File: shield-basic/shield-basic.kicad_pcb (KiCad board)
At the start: 2 copper layers, 53 x 59 mm, 58 parts, among them CON1 SD_Card, IC1 DRV8833, P1 CONN_01X04, P2 CONN_01X04, P3 CONN_01X04, P4 CONN_01X04, P5 CONN_01X04, P6 CONN_01X02, P7 CONN_01X02, P8 CONN_01X06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

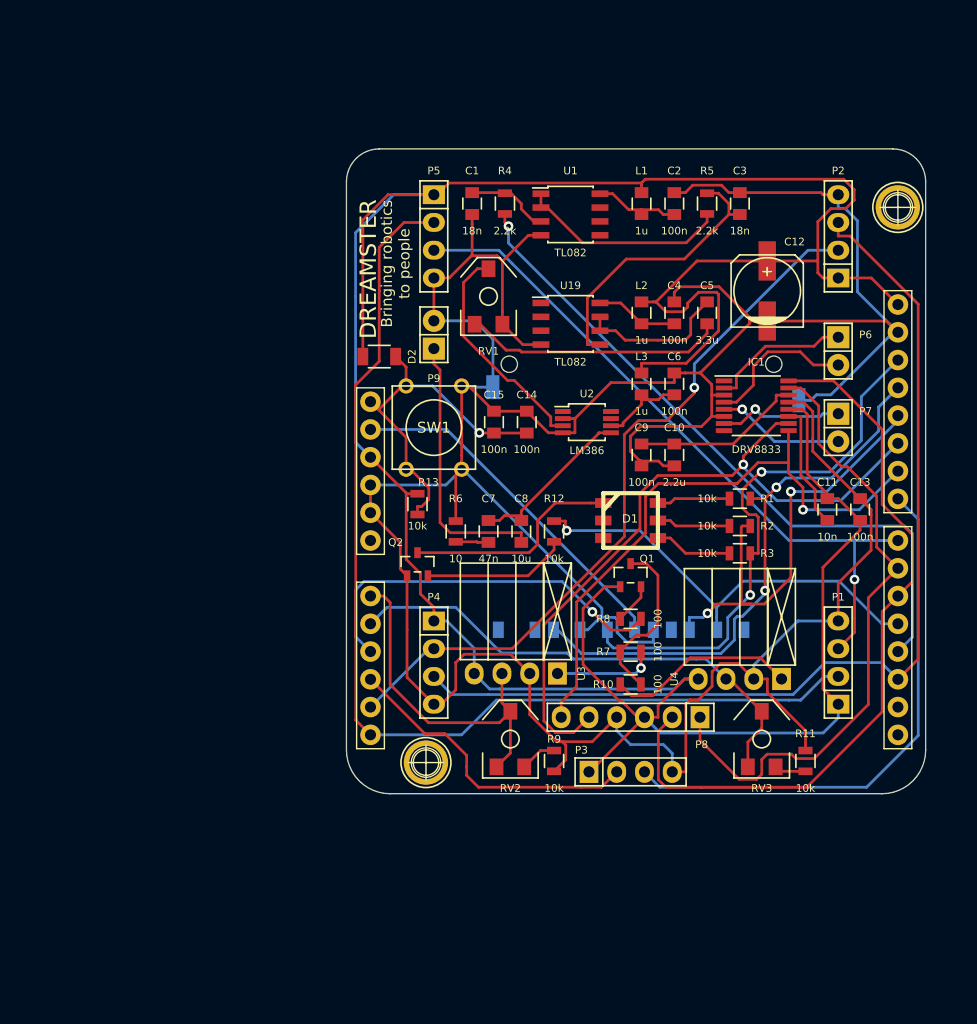
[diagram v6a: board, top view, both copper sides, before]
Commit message: The board is routed again, to fix some problems.
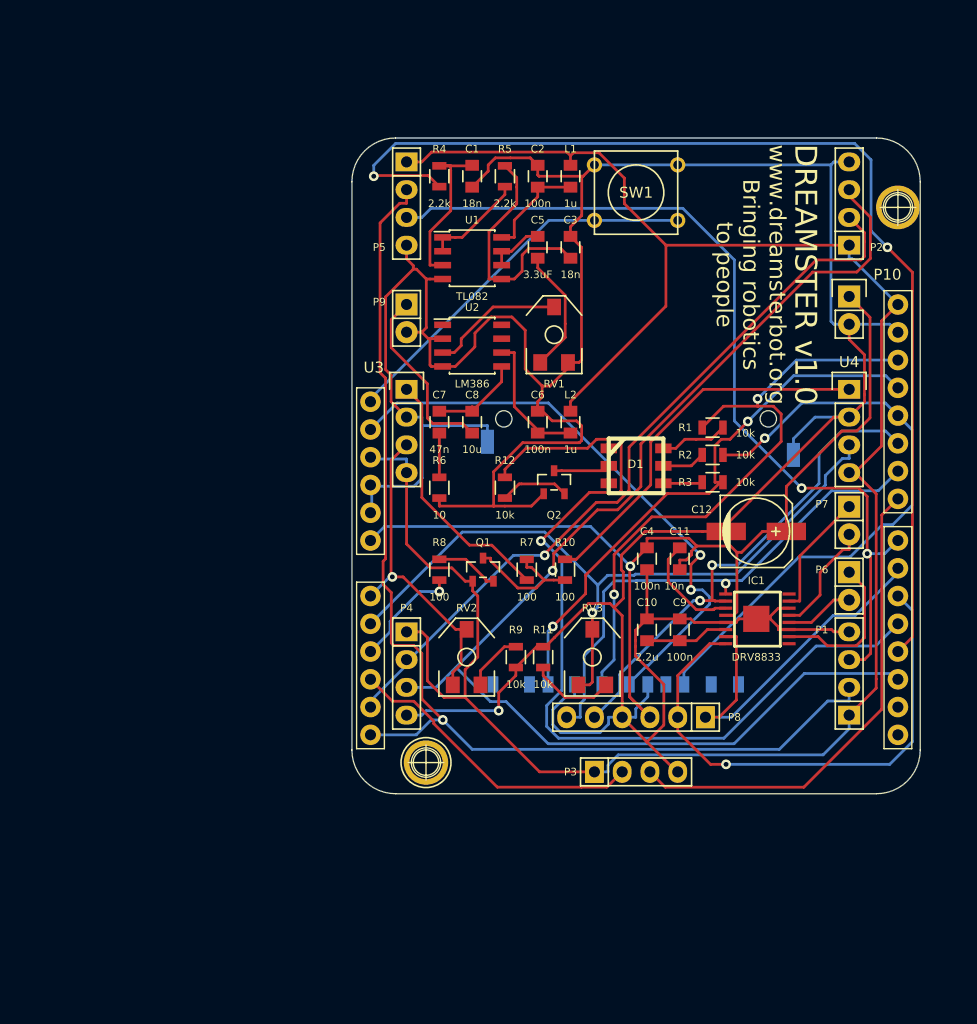
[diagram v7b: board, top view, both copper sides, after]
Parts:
- removed the 1pin at (197.9, 48.4)
- removed the 1pin at (154.8, 99.2)
- removed C13, C14, C15: 100n, Capacitors_SMD:C_0805
- removed D2: CD1206-S01575, Capacitors_SMD:C_1206
- removed L3: 1u, Capacitors_SMD:C_0805
- removed R13: 10k, Resistors_SMD:R_0805
- removed U19: TL082, Housings_SOIC:SOIC-8_3.9x4.9mm_Pitch1.27mm
- added 1pin: VAL**, Connect:1pin, F.Cu at (198.0, 48.4)
- added 1pin: VAL**, Connect:1pin, F.Cu at (154.8, 99.2)
- added P10: CONN_01X02, Socket_Strips:Socket_Strip_Straight_1x02, F.Cu at (193.5, 56.5)
- C5: value 3.3u -> 3.3uF
- IC1: footprint Housings_SSOP:TSSOP-16_4.4x5mm_Pitch0.65mm -> Dreamster:drv8833
- Q1: value PNP -> BC857
- Q2: value NPN -> BC847
- U2: footprint Housings_SSOP:MSOP-8_3x3mm_Pitch0.65mm -> Housings_SOIC:SOIC-8_3.9x4.9mm_Pitch1.27mm
- U3, U4: footprint Socket_Strips:Socket_Strip_Angled_1x04 -> Socket_Strips:Socket_Strip_Straight_1x04
- moved SW1 28.4 mm to (174.0, 47.0), turned to 180 degrees
- moved U4 28.3 mm to (193.5, 65.0), turned to 270 degrees
- moved U3 27.9 mm to (153.0, 65.0), turned to 270 degrees
- moved R11 25.8 mm to (165.5, 89.5)
- moved C4 22.6 mm to (175.0, 80.5), turned to 270 degrees
- moved C12 22.0 mm to (185.0, 78.0), turned to 0 degrees
- moved P6 21.5 mm to (193.5, 83.0)
- moved IC1 19.5 mm to (185.0, 86.0), turned to 90 degrees
- moved R5 18.7 mm to (162.0, 45.5)
- moved R8 18.1 mm to (156.0, 81.5), turned to 270 degrees
- moved RV3 17.2 mm to (170.0, 89.5)
- moved C5 16.6 mm to (165.0, 52.0)
- moved C9 16.4 mm to (178.0, 87.0), turned to 90 degrees
- moved C10 16.2 mm to (175.0, 87.0), turned to 90 degrees
- moved C3 16.0 mm to (168.0, 52.0)
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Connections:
- C11 pad 1: +5VD -> +BATT
- C12 pad 1: +5VD -> +BATT
- C4 pad 1: Net-(C4-Pad1) -> +BATT
- CON1 pad 1: /LED_enable -> (no net)
- IC1 pad 12: +5VD -> +BATT
- L2 pad 2: Net-(C4-Pad1) -> Net-(C6-Pad1)
- P8 pad 3: +5VD -> +BATT
- R1 pad 1: /RED -> /BLUE
- R3 pad 1: /BLUE -> /RED
- U1 pad 5: (no net) -> Net-(C3-Pad1)
- U1 pad 6: (no net) -> Net-(C5-Pad1)
- U1 pad 7: (no net) -> Net-(C5-Pad1)
- U5 pad VIN: (no net) -> +BATT
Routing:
- net +BATT: track 0.00 -> 96.3 mm, vias 0 -> 1
- net +5VD: track 277.6 -> 195.9 mm
- net /LED_enable: track 39.8 -> 81.7 mm
- net /sound/In: track 62.1 -> 101.5 mm, vias 1 -> 2
- net /irsensor/~EMITTER: track 34.9 -> 10.2 mm
- net /hbridge/RMI2: track 58.1 -> 33.8 mm
- net /ECHO_B: track 91.2 -> 115.2 mm, vias 0 -> 1
- net +3V3: track 32.4 -> 53.6 mm, vias 0 -> 2
- net /irsensor/RSENS: track 46.5 -> 66.3 mm, vias 0 -> 1
- net /hbridge/LMI2: track 64.1 -> 44.8 mm, vias 1 -> 2
- net /hbridge/RMI1: track 68.4 -> 49.3 mm, vias 0 -> 1
- net /ECHO_C: track 64.0 -> 82.1 mm, vias 1 -> 2
- net Net-(R10-Pad2): track 17.4 -> 34.7 mm
- net Net-(D1-Pad1): track 24.3 -> 8.20 mm
- net /GREEN: track 41.4 -> 55.6 mm, vias 2 -> 1
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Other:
- board size 53 x 59 mm -> 52 x 60 mm
- board text added: "DREAMSTER v1.0"
- board text added: "www.dreamsterbot.org Bringing robotics to people"
- board text removed: "Bringing robotics to people"
- board text removed: "DREAMSTER"

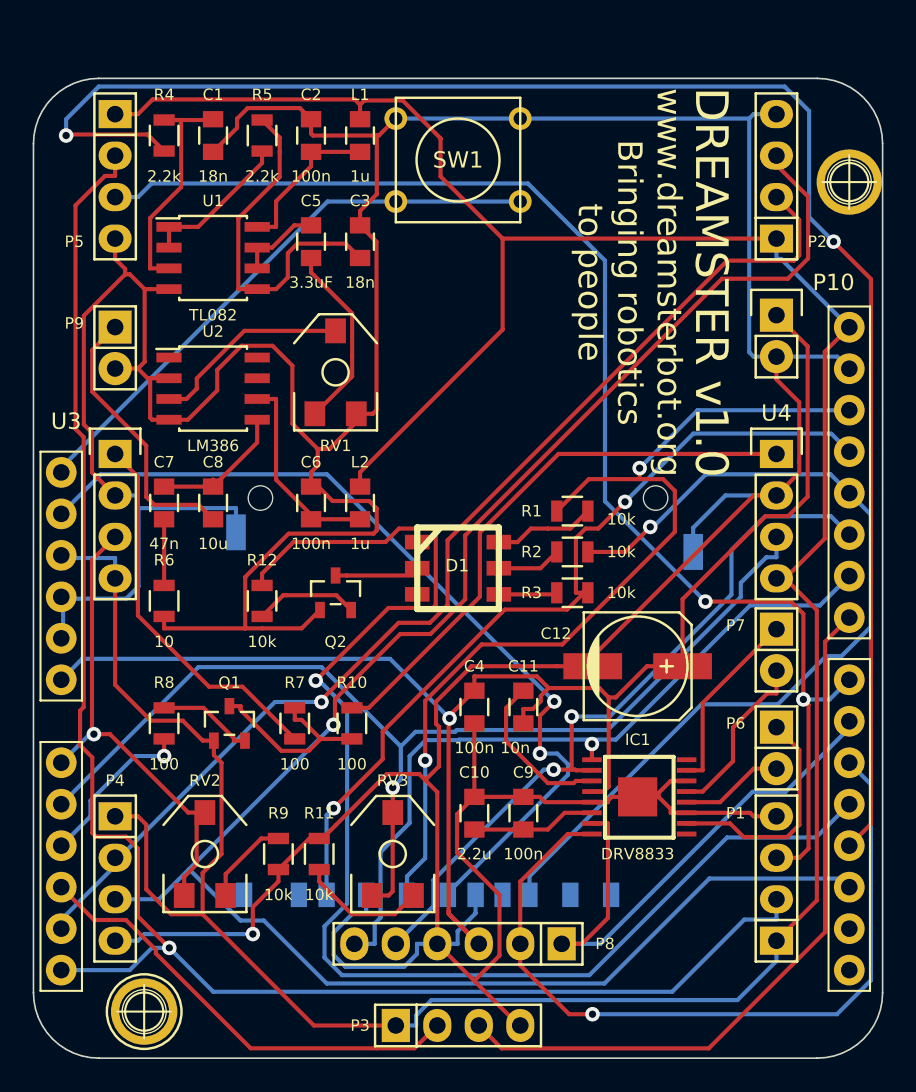
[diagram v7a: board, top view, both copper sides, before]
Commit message: Fix: #6 Add Gnd Plane. Fix: #9 Change IR footprint. Fix: #10 Move the trimmer, the orientation is ok.
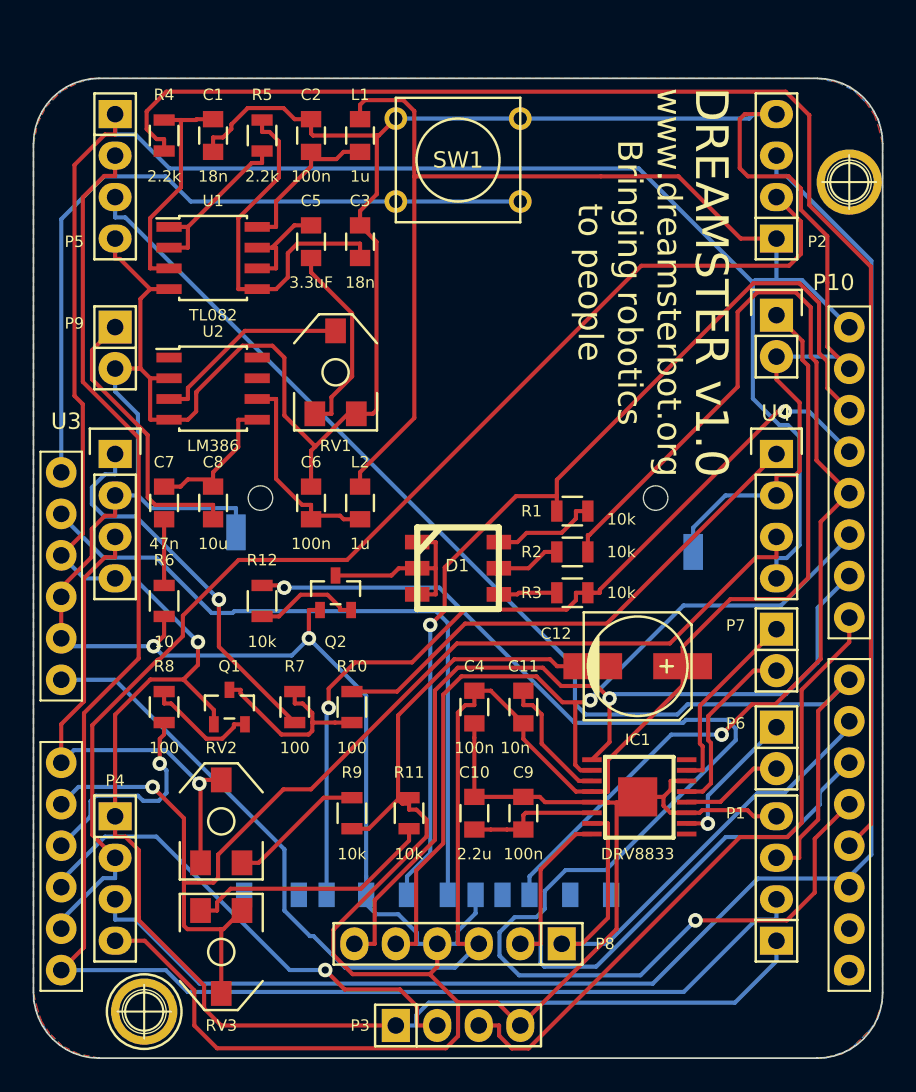
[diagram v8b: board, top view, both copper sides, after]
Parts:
- moved RV3 12.1 mm to (159.5, 95.5), turned to 180 degrees
- moved R11 6.04 mm to (171.0, 87.0)
- moved R9 5.15 mm to (167.5, 87.0)
- moved RV2 2.24 mm to (159.5, 87.5)
- moved Q1 1.00 mm to (160.0, 80.5)
- moved R10 1.00 mm to (167.5, 80.5)
- moved R7 1.00 mm to (164.0, 80.5)
- moved R8 1.00 mm to (156.0, 80.5)
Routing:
- net +5VD: track 195.9 -> 237.5 mm, vias 0 -> 1
- net /ECHO_B: track 115.2 -> 98.7 mm, vias 1 -> 0
- net /GREEN: track 55.6 -> 71.6 mm
- net /hbridge/RMI1: track 49.3 -> 36.9 mm, vias 1 -> 0
- net +3V3: track 53.6 -> 43.2 mm, vias 2 -> 0
- net /RESET: track 35.1 -> 45.3 mm
- net /sound/In: track 101.5 -> 91.7 mm, vias 2 -> 0
- net /hbridge/LMI1: track 46.3 -> 54.3 mm
- net /hbridge/LMI2: track 44.8 -> 52.6 mm, vias 2 -> 1
- net Net-(R11-Pad1): track 7.80 -> 15.6 mm
- net /ECHO_C: track 82.1 -> 74.6 mm, vias 2 -> 0
- net GND: track 332.7 -> 338.8 mm, vias 1 -> 2
- net /TRG_B: track 69.5 -> 75.0 mm, vias 1 -> 0
- net +BATT: track 96.3 -> 101.6 mm, vias 1 -> 0
- net /hbridge/RM+: track 14.1 -> 8.95 mm, vias 0 -> 1
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- added copper zone on B.Cu, net +5VD
- added copper zone on F.Cu, net GND
